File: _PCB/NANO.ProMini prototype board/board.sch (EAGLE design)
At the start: 64 parts, among them T1_5MM 5mm, T2_5MM 5mm, T3_5MM 5mm

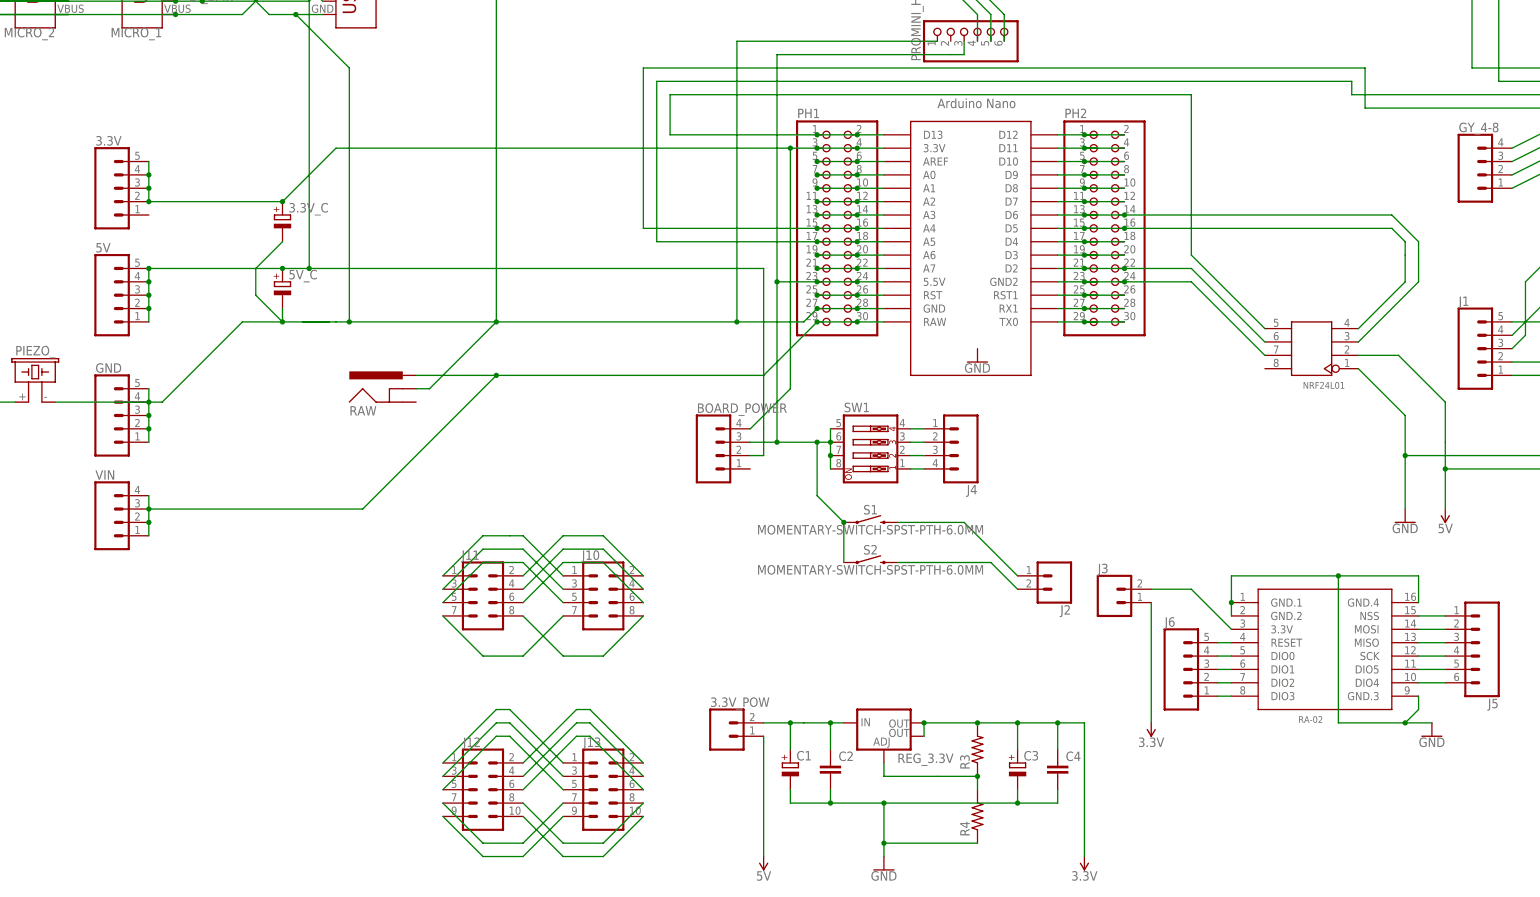
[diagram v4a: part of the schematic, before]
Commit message: ESP8266 support
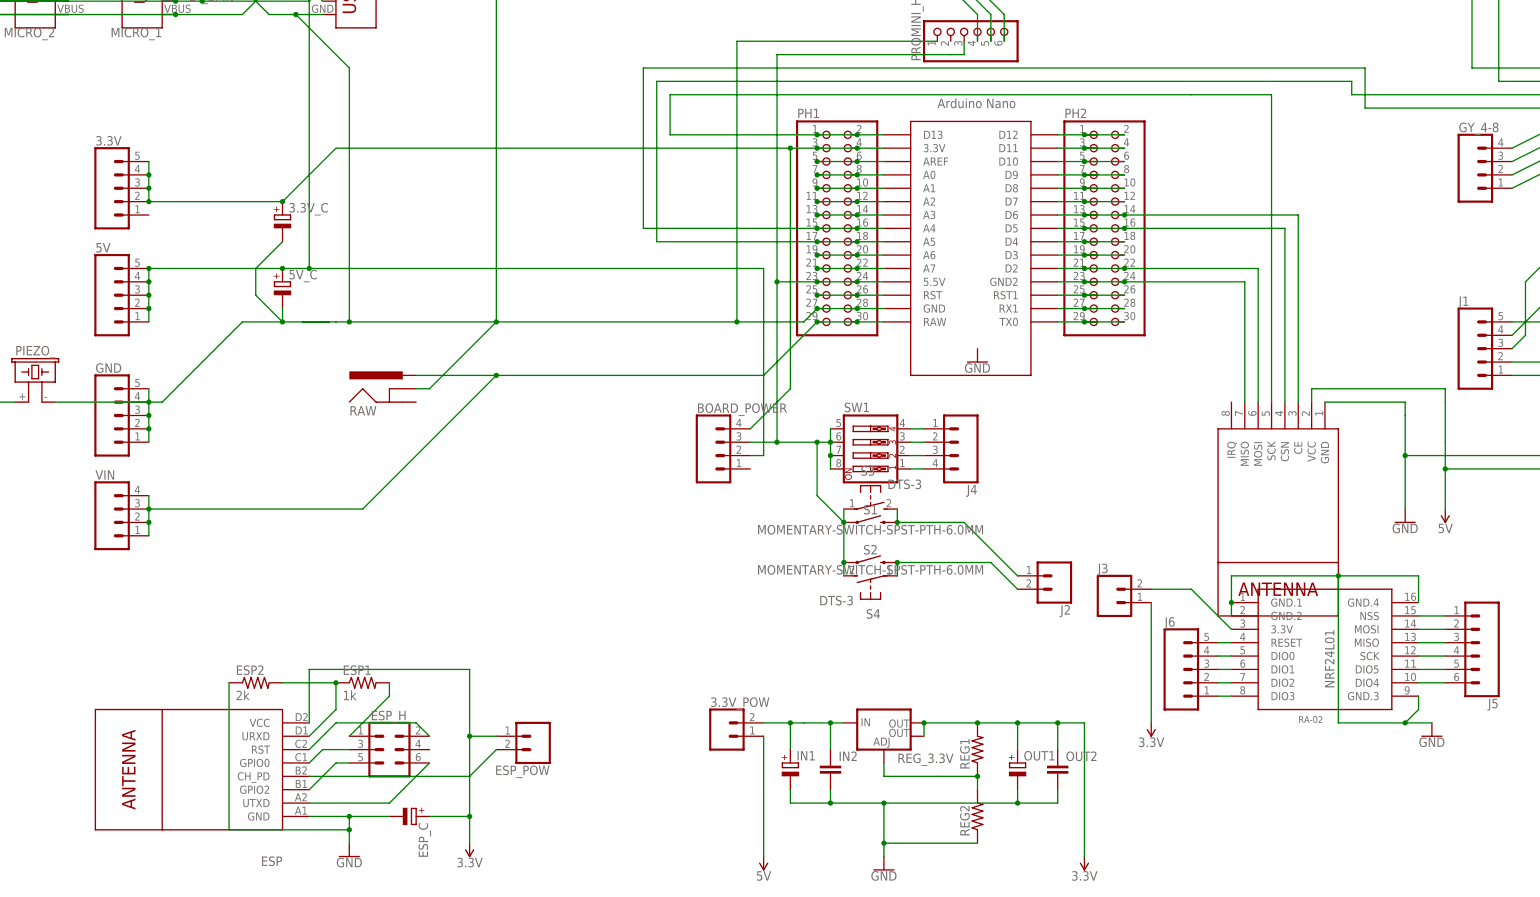
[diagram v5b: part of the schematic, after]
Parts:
- removed J10, J11: (no value), SparkFun-Connectors:CONN_04X2
- removed J12, J13: (no value), SparkFun-Connectors:CONN_05X2PTH
- added ESP: WIRELESS-WIFI-ESP-01, diy-modules:WIRELESS-WIFI-ESP-01
- added ESP1: 1k, rcl:R-US_0207/7
- added ESP2: 2k, rcl:R-US_0207/7
- added ESP_C: (no value), rcl:CPOL-EUE2.5-5
- added ESP_H: (no value), SparkFun-Connectors:CONN_03X2FEMALE
- added ESP_POW: (no value), SparkFun-Connectors:CONN_02LOCK
- added S3, S4: DTS-3, switch-tact:DTS-3
- NRF24L01: value (none) -> WIRELESS-NRF24L01; device Seeed-Connector:DIP-BLACK-FEMALE-HEADER(2X4P-2.54) -> diy-modules:WIRELESS-NRF24L01
- renumbered C1 to IN1, C2 to IN2, C3 to OUT1, C4 to OUT2, R3 to REG1, R4 to REG2
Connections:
- removed net N$65: J10.8, J11.8
- removed net N$66: J12.1, J13.1
- removed net N$67: J12.3, J13.3
- removed net N$68: J12.5, J13.5
- removed net N$69: J12.9, J13.9
- removed net N$70: J12.7, J13.7
- removed net N$71: J12.2, J13.2
- removed net N$72: J12.4, J13.4
- removed net N$73: J12.6, J13.6
- removed net N$74: J12.10, J13.10
- removed net N$75: J12.8, J13.8
- net 3.3V: now also ESP.VCC, ESP_C.+, ESP_POW.1
- net 5V: now also NRF24L01.VCC; no longer NRF24L01.2
- net CE_NRF: now also NRF24L01.CE; no longer NRF24L01.3
- net CSN_NRF: now also NRF24L01.CSN; no longer NRF24L01.4
- net GND: now also ESP.GND, ESP2.1, ESP_C.-, NRF24L01.GND; no longer NRF24L01.1
- net MISO_NRF: now also NRF24L01.MISO; no longer NRF24L01.7
- net MOSI_NRF: now also NRF24L01.MOSI; no longer NRF24L01.6
- net N$36: now also S3.1, S4.2
- net N$37: now also S3.2
- net N$43: now also S4.1
- net N$55: now also ESP.CH_PD, ESP_POW.2; no longer J10.1, J11.1
- net N$58: now also ESP.URXD, ESP1.1, ESP2.2; no longer J10.3, J11.3
- net N$59: now also ESP.RST, ESP_H.2; no longer J10.5, J11.5
- net N$60: now also ESP.GPIO0, ESP_H.3; no longer J10.7, J11.7
- net N$61: now also ESP1.2, ESP_H.1; no longer J10.2, J11.2
- net N$63: now also ESP.GPIO2, ESP_H.5; no longer J10.4, J11.4
- net N$64: now also ESP.UTXD, ESP_H.6; no longer J10.6, J11.6
- net SCK_NRF: now also NRF24L01.SCK; no longer NRF24L01.5

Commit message: prototype board finished
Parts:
- removed 3.3V_POW: (no value), SparkFun-Connectors:CONN_02LOCK_LONGPADS
- removed IN1, OUT1: (no value), rcl:CPOL-EUE2.5-5
- removed IN2, OUT2: (no value), rcl:C-EU025-030X050
- removed REG1, REG2: (no value), rcl:R-US_0207/7
- removed REG_3.3V: (no value), SparkFun-IC-Power:V_REG_LM1117SOT223
- removed R_SHIELD: 10k, rcl:R-US_0207/7
- renumbered ESP to ESP8266
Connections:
- removed net N$77: 3.3V_POW.2, IN1.+, IN2.1, REG_3.3V.IN
- removed net N$79: REG1.1, REG2.2, REG_3.3V.ADJ
- removed net SHIELD_IN: MICRO_1.SHIELD, MICRO_2.SHIELD, MINI_1.SHIELD, R_SHIELD.1, USB_B.SHIELD
- net 3.3V: now also 3.3V.1; no longer OUT1.+, OUT2.1, REG1.2, REG_3.3V.OUT, REG_3.3V.OUT@1
- net 5V: no longer 3.3V_POW.1
- net GND: no longer IN1.-, IN2.2, OUT1.-, OUT2.2, REG2.1, R_SHIELD.2
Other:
- moved on the sheet: J3, J5, J6, RA-02

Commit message: final prototype
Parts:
- added PAD1, PAD10, PAD2, PAD3, PAD4, PAD5, PAD6, PAD7, PAD8, PAD9: (no value), wirepad:SMD2
- added U$1: USB-SERIAL-FT232R, diy-modules:USB-SERIAL-FT232R
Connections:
- removed net N$56: CP2102_USB-SERIAL.DTR, J7.2, J9.2, PROMINI_H.6
- new net N$65: BOARD_POWER.1, PAD10.P
- new net N$66: CP2102_USB-SERIAL.DTR, J7.6, J9.2, PROMINI_H.6, U$1.DTR
- net 3.3V: now also J7.2, PAD1.P, PAD3.P, PAD5.P, PAD7.P; no longer J7.1
- net 5V: now also J7.3, PAD8.P, U$1.VCC; no longer J7.6
- net GND: now also J7.1, U$1.GND; no longer J7.5
- net N$36: now also PAD9.P
- net N$55: now also PAD2.P, PAD6.P
- net N$57: now also J7.5, U$1.RX; no longer J7.3
- net N$62: now also U$1.TX
- net N$76: now also PAD4.P
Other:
- moved on the sheet: B1, J7, PIN1, PIN2, PIN3, T1_5MM, T2_5MM, T3_5MM
